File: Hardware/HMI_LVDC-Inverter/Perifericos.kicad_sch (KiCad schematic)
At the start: 41 parts, among them J11 Conn_01x04_Pin, K1 RT174012, Q1 BC847, Q2 2N7002, SW2 SW_MEC_5G, SW3 SW_MEC_5G, SW4 SW_MEC_5G, SW5 SW_MEC_5G, SW6 SW_MEC_5G, SW7 SW_MEC_5G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

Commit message: Agregado y corrección de borneras
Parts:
- removed J11: Conn_01x04_Pin, Connector_PinHeader_1.00mm:PinHeader_1x04_P1.00mm_Vertical, symbol Connector:Conn_01x04_Pin
- added J5: OLED, Connector_JST:JST_XH_B4B-XH-A_1x04_P2.50mm_Vertical, symbol Connector_Generic:Conn_01x04
- SW2, SW3, SW4, SW5, SW6, SW7, SW8, SW9: footprint (none) -> Footprints:SW_Push_SPST_NO_Alps_SKRK; Compra https://www.lcsc.com/product-detail/C2894750.html -> https://www.lcsc.com/product-detail/C720478.html?s_z=n_TS-1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; Price 0.1224 -> 0.0603
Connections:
- net +3.3V_ESP: now also J5.2 (Pin_2)
- net GND: now also J5.1 (Pin_1)
- net Matrix_0: no longer SW2.2 (A), SW3.2 (A), SW4.2 (A), SW5.2 (A)
- net Matrix_1: no longer SW6.2 (A), SW7.2 (A), SW8.2 (A), SW9.2 (A)
- net Matrix_2: now also SW2.2 (B), SW6.2 (B); no longer SW2.3 (B), SW2.4 (B), SW6.3 (B), SW6.4 (B)
- net Matrix_3: now also SW3.2 (B), SW7.2 (B); no longer SW3.3 (B), SW3.4 (B), SW7.3 (B), SW7.4 (B)
- net Matrix_4: now also SW4.2 (B), SW8.2 (B); no longer SW4.3 (B), SW4.4 (B), SW8.3 (B), SW8.4 (B)
- net Matrix_5: now also SW5.2 (B), SW9.2 (B); no longer SW5.3 (B), SW5.4 (B), SW9.3 (B), SW9.4 (B)
- net OLED_SCL: now also J5.3 (Pin_3)
- net OLED_SDA: now also J5.4 (Pin_4)

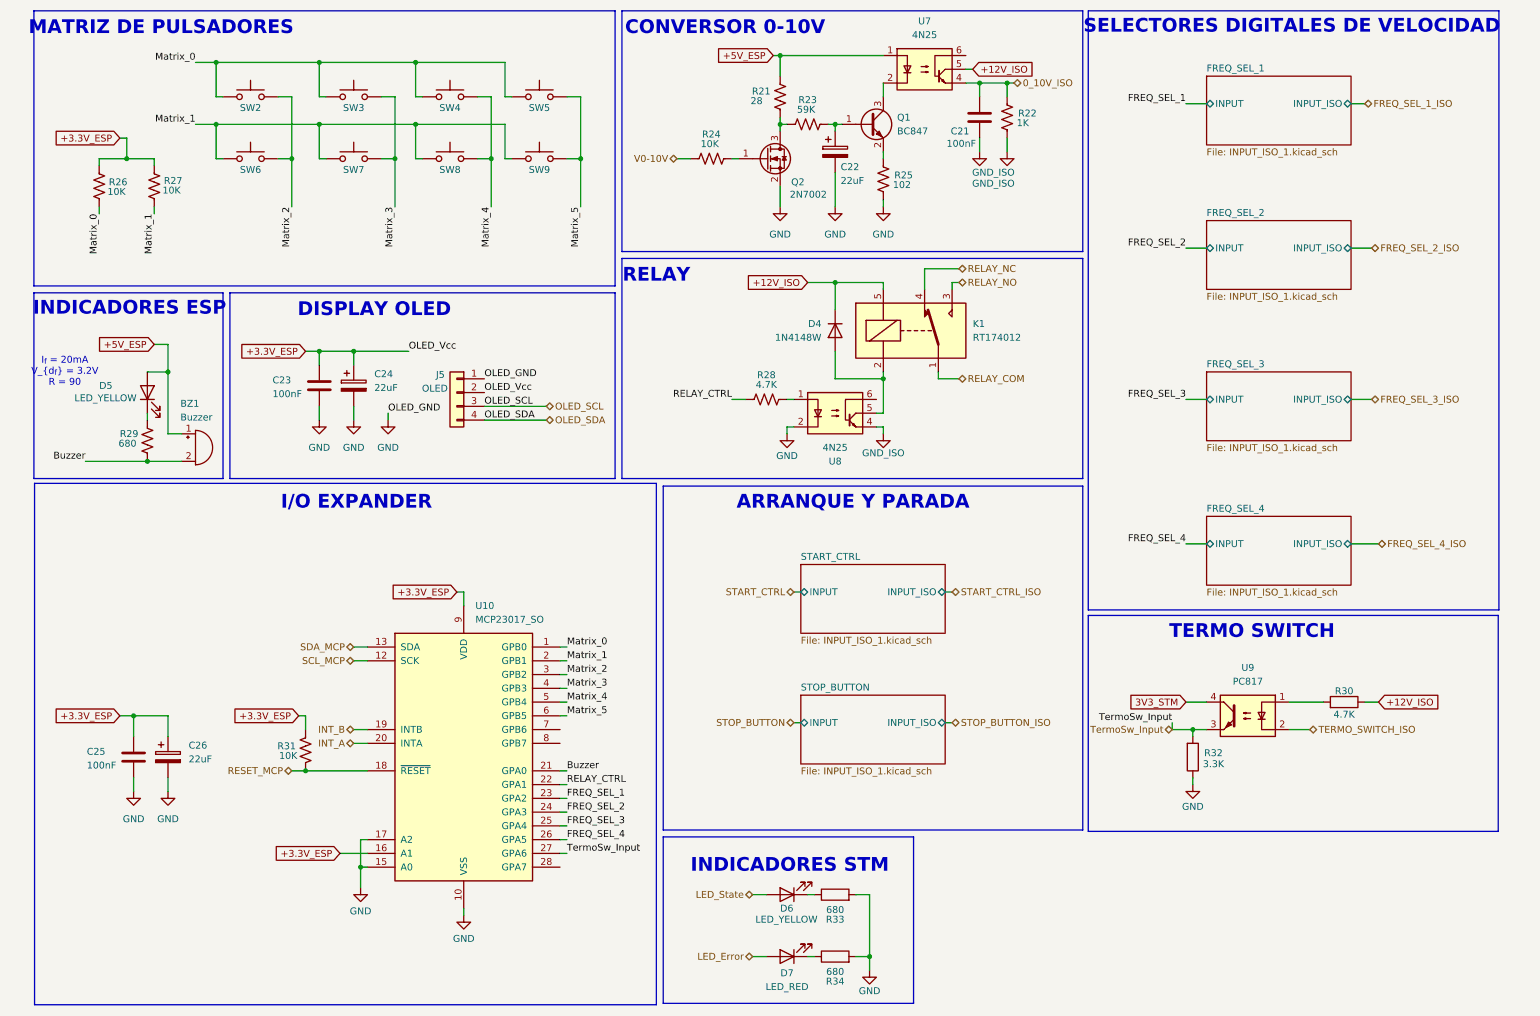
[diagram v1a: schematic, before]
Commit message: Terminada la placa del HMI con revisión de reglas de diseño
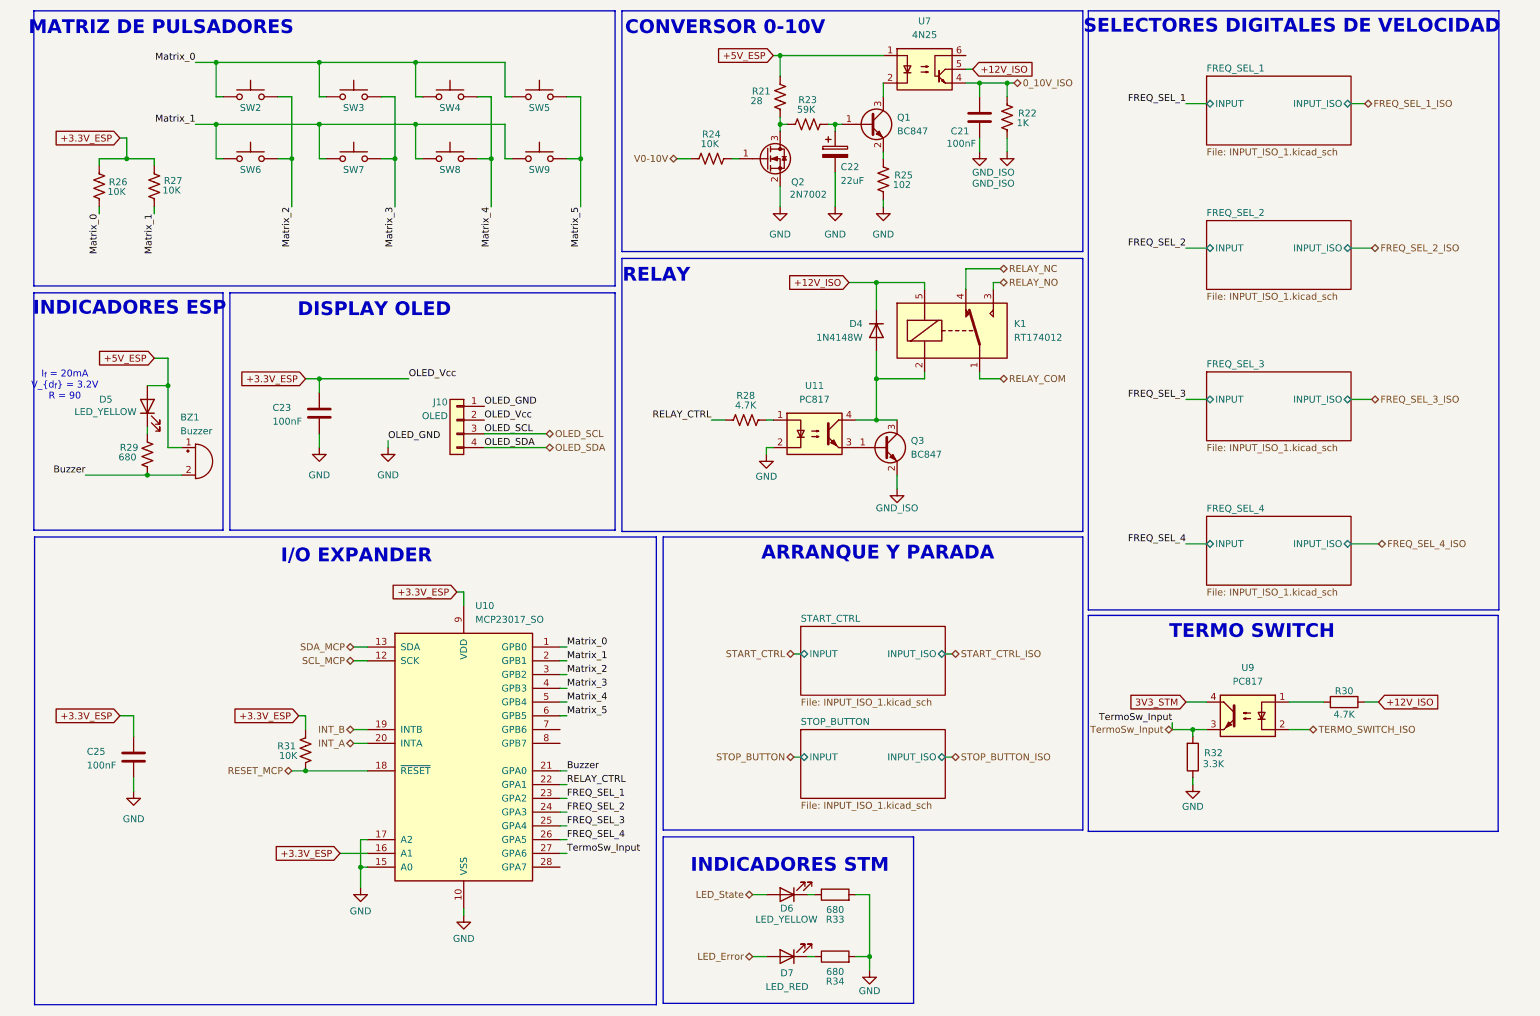
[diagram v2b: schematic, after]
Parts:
- removed C24, C26: 22uF, Capacitor_SMD:CP_Elec_5x5.4, symbol Device:C_Polarized
- removed U8: 4N25, Package_DIP:DIP-6_W7.62mm_SMDSocket_SmallPads, symbol Isolator:4N25
- added Q3: BC847, Package_TO_SOT_SMD:SOT-523, symbol Transistor_BJT:BC847
- added U11: PC817, Package_DIP:DIP-4_W7.62mm_SMDSocket_SmallPads, symbol Isolator:PC817
- J10: renamed from J5; footprint Connector_JST:JST_XH_B4B-XH-A_1x04_P2.50mm_Vertical -> Footprints:Display OLED
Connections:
- net GND: now also U11.2
- net GND_ISO: now also Q3.2 (E)
- net at D4.2 (A), K1.2: now also Q3.3 (C), U11.4
- net at R28.2: now also U11.1
- new net: Q3.1 (B), U11.3
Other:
- moved on the sheet: BZ1, C23, D4, D5, J10, K1, R28, R29
